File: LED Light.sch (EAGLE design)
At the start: 17 parts, among them J1 AVR_SPI_PRG_6NS, U1 Tiny85-20-SMT

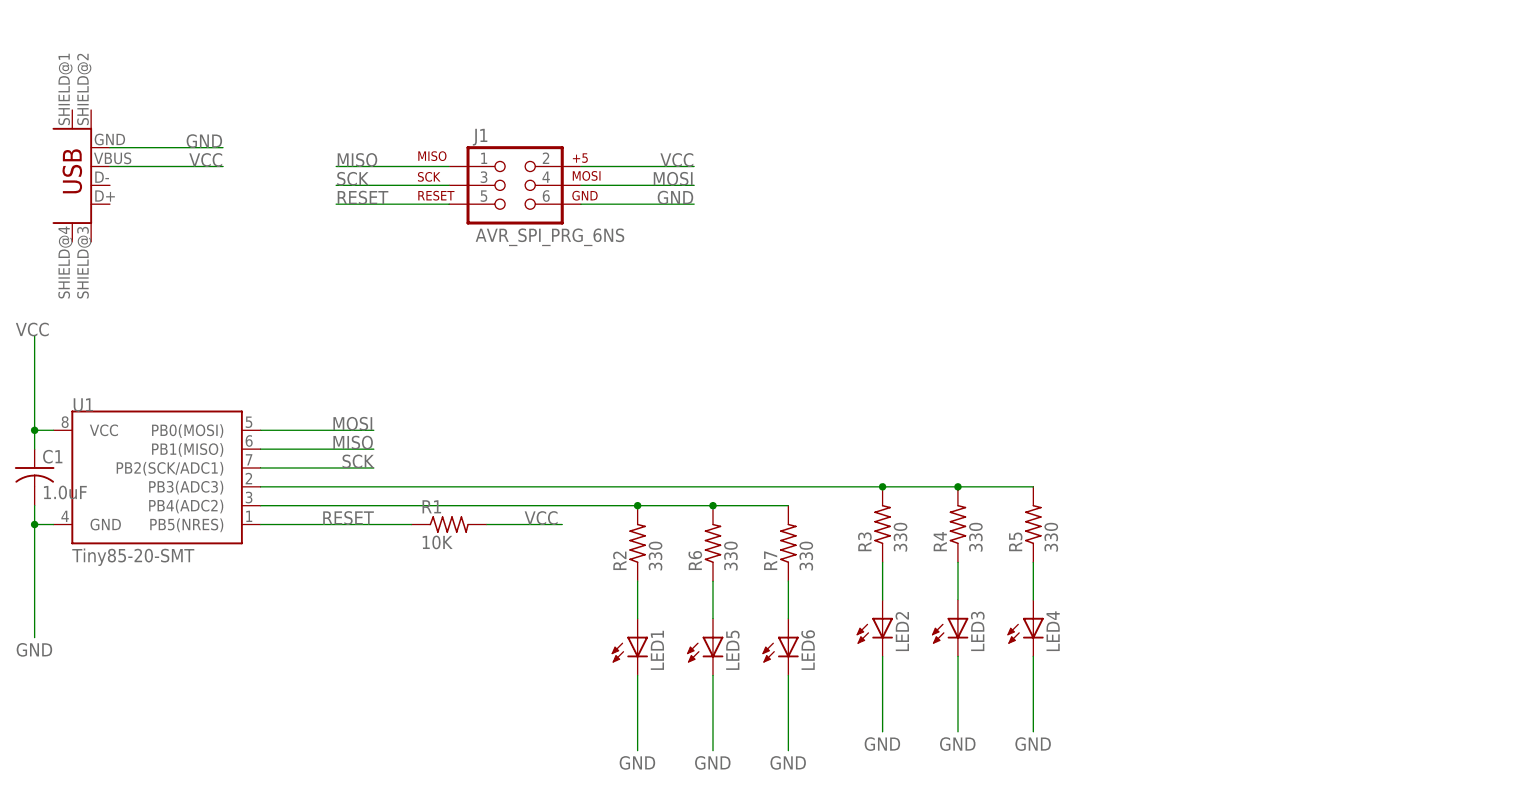
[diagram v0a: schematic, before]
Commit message: Finish initial version of Pac Man board. Generate PNGs for milling.
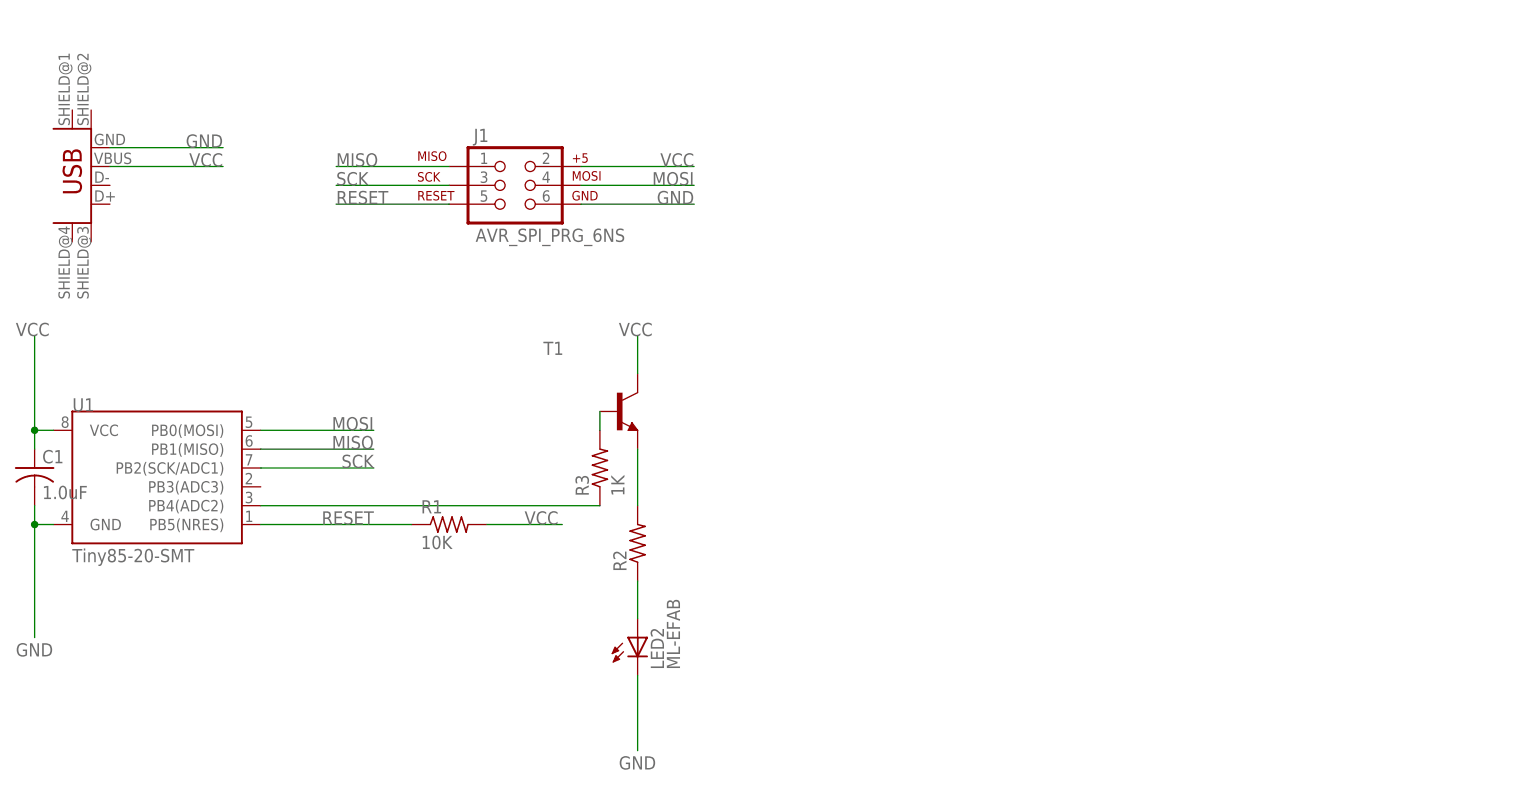
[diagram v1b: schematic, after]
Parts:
- removed LED1, LED3, LED4, LED5, LED6: (no value), led:LEDSMT1206
- removed R4, R5, R6, R7: 330, rcl:R-US_R1206
- added T1: (no value), transistor:MMBT3904LT1-NPN-SOT23-BEC
- JP1: value USB_MINIB -> USB_MINIB-POWER; device fab:USB_MINIB -> LED Light:USB_MINIB-POWER
- LED2: value (none) -> ML-EFAB; device led:LEDSMT1206 -> LED Light:ML-EFAB
- R2: value 330 -> (none)
- R3: value 330 -> 1K
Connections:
- removed net N$5: LED6.A, R7.1
- removed net N$6: LED5.A, R6.1
- removed net N$7: LED3.A, R4.1
- removed net N$8: LED4.A, R5.1
- net GND: now also LED2G$1.C@1; no longer LED1.C, LED2.C, LED3.C, LED4.C, LED5.C, LED6.C
- net N$1: now also T1.E; no longer R6.2, R7.2, U1.PB4(ADC2)
- net N$2: now also T1.B; no longer R4.2, R5.2, U1.PB3(ADC3)
- net N$3: now also LED2G$1.A@1; no longer LED1.A
- net N$4: now also U1.PB4(ADC2); no longer LED2.A
- net VCC: now also T1.C
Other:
- moved on the sheet: R3
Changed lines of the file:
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@@
 <part name="J1" library="SparkFun-Connectors" deviceset="AVR_SPI_PRG_6" device="NS"/>
 <part name="R1" library="rcl" deviceset="R-US_" device="R1206" value="10K"/>
-<part name="R2" library="rcl" deviceset="R-US_" device="R1206" value="330"/>
-<part name="R3" library="rcl" deviceset="R-US_" device="R1206" value="330"/>
-<part name="LED1" library="led" deviceset="LED" device="SMT1206"/>
-<part name="LED2" library="led" deviceset="LED" device="SMT1206"/>
-<part name="JP1" library="fab" deviceset="USB_MINIB" device=""/>
+<part name="R2" library="rcl" deviceset="R-US_" device="R1206"/>
+<part name="JP1" library="LED Light" deviceset="USB_MINIB" device="-POWER"/>
 <part name="C1" library="rcl" deviceset="C-US" device="C1206" value="1.0uF"/>
-<part name="R4" library="rcl" deviceset="R-US_" device="R1206" value="330"/>
-<part name="LED3" library="led" deviceset="LED" device="SMT1206"/>
-<part name="R5" library="rcl" deviceset="R-US_" device="R1206" value="330"/>
-<part name="LED4" library="led" deviceset="LED" device="SMT1206"/>
-<part name="R6" library="rcl" deviceset="R-US_" device="R1206" value="330"/>
-<part name="R7" library="rcl" deviceset="R-US_" device="R1206" value="330"/>
-<part name="LED5" library="led" deviceset="LED" device="SMT1206"/>
-<part name="LED6" library="led" deviceset="LED" device="SMT1206"/>
+<part name="LED2" library="LED Light" deviceset="ML-E" device="FAB"/>
+<part name="T1" library="transistor" deviceset="*-NPN-" device="SOT23-BEC" technology="MMBT3904LT1"/>
+<part name="R3" library="rcl" deviceset="R-US_" device="R1206" value="1K"/>
 </parts>
 <sheets>
@@
 <instance part="R1" gate="G$1" x="66.04" y="33.02"/>
 <instance part="R2" gate="G$1" x="91.44" y="30.48" rot="R90"/>
-<instance part="R3" gate="G$1" x="124.46" y="33.02" rot="R90"/>
-<instance part="LED1" gate="G$1" x="91.44" y="17.78"/>
-<instance part="LED2" gate="G$1" x="124.46" y="20.32"/>
 <instance part="JP1" gate="G$1" x="17.78" y="78.74" rot="R180"/>
 <instance part="C1" gate="G$1" x="10.16" y="40.64"/>
-<instance part="R4" gate="G$1" x="134.62" y="33.02" rot="R90"/>
-<instance part="LED3" gate="G$1" x="134.62" y="20.32"/>
-<instance part="R5" gate="G$1" x="144.78" y="33.02" rot="R90"/>
-<instance part="LED4" gate="G$1" x="144.78" y="20.32"/>
-<instance part="R6" gate="G$1" x="101.6" y="30.48" rot="R90"/>
-<instance part="R7" gate="G$1" x="111.76" y="30.48" rot="R90"/>
-<instance part="LED5" gate="G$1" x="101.6" y="17.78"/>
-<instance part="LED6" gate="G$1" x="111.76" y="17.78"/>
+<instance part="LED2" gate="G$1" x="91.44" y="15.24"/>
+<instance part="T1" gate="G$1" x="88.9" y="48.26"/>
+<instance part="R3" gate="G$1" x="86.36" y="40.64" rot="R90"/>
 </instances>
 <busses>
@@
 <wire x1="20.32" y1="81.28" x2="35.56" y2="81.28" width="0.1524" layer="91"/>
 <label x="35.56" y="81.28" size="1.778" layer="95" rot="MR0"/>
+</segment>
+<segment>
+<pinref part="T1" gate="G$1" pin="C"/>
+<wire x1="91.44" y1="53.34" x2="91.44" y2="58.42" width="0.1524" layer="91"/>
+<label x="88.9" y="58.42" size="1.778" layer="95"/>
 </segment>
 </net>
@@
 </segment>
 <segment>
-<pinref part="LED1" gate="G$1" pin="C"/>
 <wire x1="91.44" y1="12.7" x2="91.44" y2="2.54" width="0.1524" layer="91"/>
 <label x="88.9" y="0" size="1.778" layer="95"/>
-</segment>
-<segment>
-<pinref part="LED2" gate="G$1" pin="C"/>
-<wire x1="124.46" y1="15.24" x2="124.46" y2="5.08" width="0.1524" layer="91"/>
-<label x="121.92" y="2.54" size="1.778" layer="95"/>
-</segment>
-<segment>
-<pinref part="LED3" gate="G$1" pin="C"/>
-<wire x1="134.62" y1="15.24" x2="134.62" y2="5.08" width="0.1524" layer="91"/>
-<label x="132.08" y="2.54" size="1.778" layer="95"/>
-</segment>
-<segment>
-<pinref part="LED4" gate="G$1" pin="C"/>
-<wire x1="144.78" y1="15.24" x2="144.78" y2="5.08" width="0.1524" layer="91"/>
-<label x="142.24" y="2.54" size="1.778" layer="95"/>
-</segment>
-<segment>
-<pinref part="LED5" gate="G$1" pin="C"/>
-<wire x1="101.6" y1="12.7" x2="101.6" y2="2.54" width="0.1524" layer="91"/>
-<label x="99.06" y="0" size="1.778" layer="95"/>
-</segment>
-<segment>
-<pinref part="LED6" gate="G$1" pin="C"/>
-<wire x1="111.76" y1="12.7" x2="111.76" y2="2.54" width="0.1524" layer="91"/>
-<label x="109.22" y="0" size="1.778" layer="95"/>
+<pinref part="LED2" gate="G$1" pin="C@1"/>
 </segment>
 </net>
@@
 </segment>
 </net>
+<net name="N$3" class="0">
+<segment>
+<pinref part="R2" gate="G$1" pin="1"/>
+<wire x1="91.44" y1="20.32" x2="91.44" y2="25.4" width="0.1524" layer="91"/>
+<pinref part="LED2" gate="G$1" pin="A@1"/>
+</segment>
+</net>
 <net name="N$1" class="0">
 <segment>
-<pinref part="U1" gate="G$1" pin="PB4(ADC2)"/>
-<wire x1="40.64" y1="35.56" x2="91.44" y2="35.56" width="0.1524" layer="91"/>
 <pinref part="R2" gate="G$1" pin="2"/>
-<pinref part="R6" gate="G$1" pin="2"/>
-<wire x1="91.44" y1="35.56" x2="101.6" y2="35.56" width="0.1524" layer="91"/>
-<junction x="91.44" y="35.56"/>
-<pinref part="R7" gate="G$1" pin="2"/>
-<wire x1="101.6" y1="35.56" x2="111.76" y2="35.56" width="0.1524" layer="91"/>
-<junction x="101.6" y="35.56"/>
+<pinref part="T1" gate="G$1" pin="E"/>
+<wire x1="91.44" y1="43.18" x2="91.44" y2="35.56" width="0.1524" layer="91"/>
 </segment>
 </net>
 <net name="N$2" class="0">
 <segment>
-<pinref part="U1" gate="G$1" pin="PB3(ADC3)"/>
-<wire x1="40.64" y1="38.1" x2="124.46" y2="38.1" width="0.1524" layer="91"/>
+<pinref part="T1" gate="G$1" pin="B"/>
 <pinref part="R3" gate="G$1" pin="2"/>
-<pinref part="R4" gate="G$1" pin="2"/>
-<wire x1="124.46" y1="38.1" x2="134.62" y2="38.1" width="0.1524" layer="91"/>
-<junction x="124.46" y="38.1"/>
-<pinref part="R5" gate="G$1" pin="2"/>
-<wire x1="134.62" y1="38.1" x2="144.78" y2="38.1" width="0.1524" layer="91"/>
-<junction x="134.62" y="38.1"/>
-</segment>
-</net>
-<net name="N$3" class="0">
-<segment>
-<pinref part="R2" gate="G$1" pin="1"/>
-<pinref part="LED1" gate="G$1" pin="A"/>
-<wire x1="91.44" y1="20.32" x2="91.44" y2="25.4" width="0.1524" layer="91"/>
+<wire x1="86.36" y1="48.26" x2="86.36" y2="45.72" width="0.1524" layer="91"/>
 </segment>
 </net>
 <net name="N$4" class="0">
 <segment>
+<pinref part="U1" gate="G$1" pin="PB4(ADC2)"/>
 <pinref part="R3" gate="G$1" pin="1"/>
-<pinref part="LED2" gate="G$1" pin="A"/>
-<wire x1="124.46" y1="22.86" x2="124.46" y2="27.94" width="0.1524" layer="91"/>
+<wire x1="40.64" y1="35.56" x2="86.36" y2="35.56" width="0.1524" layer="91"/>
 </segment>
 </net>
-<net name="N$7" class="0">
-<segment>
-<pinref part="R4" gate="G$1" pin="1"/>
-<pinref part="LED3" gate="G$1" pin="A"/>
-<wire x1="134.62" y1="27.94" x2="134.62" y2="22.86" width="0.1524" layer="91"/>
-</segment>
-</net>
-<net name="N$8" class="0">
-<segment>
-<pinref part="R5" gate="G$1" pin="1"/>
-<pinref part="LED4" gate="G$1" pin="A"/>
-<wire x1="144.78" y1="27.94" x2="144.78" y2="22.86" width="0.1524" layer="91"/>
-</segment>
-</net>
-<net name="N$5" class="0">
-<segment>
-<pinref part="R7" gate="G$1" pin="1"/>
-<pinref part="LED6" gate="G$1" pin="A"/>
-<wire x1="111.76" y1="25.4" x2="111.76" y2="20.32" width="0.1524" layer="91"/>
-</segment>
-</net>
-<net name="N$6" class="0">
-<segment>
-<pinref part="R6" gate="G$1" pin="1"/>
-<pinref part="LED5" gate="G$1" pin="A"/>
-<wire x1="101.6" y1="25.4" x2="101.6" y2="20.32" width="0.1524" layer="91"/>
-</segment>
-</net>

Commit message: Night-light lamp, including PNGs for milling and PDFs for laser-cutting.
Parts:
- added LED1: ML-EFAB, LED Light:ML-EFAB
- added R4: (no value), rcl:R-US_R1206
- added R6: 49.9K, rcl:R-US_R1206
- added U$1: PHOTOTRANSISTOR-NPN-OP580AD, LED Light:PHOTOTRANSISTOR-NPN-OP580AD
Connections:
- new net N$5: LED1G$1.A@1, R4.1
- new net N$7: R6.1, U$1.C, U1.PB3(ADC3)
- net GND: now also LED1G$1.C@1, U$1.E
- net N$1: now also R4.2
- net VCC: now also R6.2
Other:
- moved on the sheet: J1
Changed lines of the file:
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@@
 <part name="T1" library="transistor" deviceset="*-NPN-" device="SOT23-BEC" technology="MMBT3904LT1"/>
 <part name="R3" library="rcl" deviceset="R-US_" device="R1206" value="1K"/>
+<part name="R4" library="rcl" deviceset="R-US_" device="R1206"/>
+<part name="LED1" library="LED Light" deviceset="ML-E" device="FAB"/>
+<part name="U$1" library="LED Light" deviceset="PHOTOTRANSISTOR-NPN" device="-OP580AD"/>
+<part name="R6" library="rcl" deviceset="R-US_" device="R1206" value="49.9K"/>
 </parts>
 <sheets>
@@
 <instances>
 <instance part="U1" gate="G$1" x="27.94" y="38.1"/>
-<instance part="J1" gate="G$1" x="73.66" y="78.74"/>
+<instance part="J1" gate="G$1" x="88.9" y="88.9"/>
 <instance part="R1" gate="G$1" x="66.04" y="33.02"/>
 <instance part="R2" gate="G$1" x="91.44" y="30.48" rot="R90"/>
@@
 <instance part="T1" gate="G$1" x="88.9" y="48.26"/>
 <instance part="R3" gate="G$1" x="86.36" y="40.64" rot="R90"/>
+<instance part="R4" gate="G$1" x="106.68" y="30.48" rot="R90"/>
+<instance part="LED1" gate="G$1" x="106.68" y="15.24"/>
+<instance part="U$1" gate="G$1" x="76.2" y="50.8"/>
+<instance part="R6" gate="G$1" x="76.2" y="60.96" rot="R90"/>
 </instances>
 <busses>
@@
 <segment>
 <pinref part="J1" gate="G$1" pin="2"/>
-<wire x1="83.82" y1="81.28" x2="99.06" y2="81.28" width="0.1524" layer="91"/>
-<label x="99.06" y="81.28" size="1.778" layer="95" rot="MR0"/>
+<wire x1="99.06" y1="91.44" x2="114.3" y2="91.44" width="0.1524" layer="91"/>
+<label x="114.3" y="91.44" size="1.778" layer="95" rot="MR0"/>
 </segment>
 <segment>
@@
 <label x="88.9" y="58.42" size="1.778" layer="95"/>
 </segment>
+<segment>
+<pinref part="R6" gate="G$1" pin="2"/>
+<wire x1="76.2" y1="66.04" x2="76.2" y2="71.12" width="0.1524" layer="91"/>
+<label x="73.66" y="71.12" size="1.778" layer="95"/>
+</segment>
 </net>
 <net name="MOSI" class="0">
 <segment>
 <pinref part="J1" gate="G$1" pin="4"/>
-<wire x1="83.82" y1="78.74" x2="99.06" y2="78.74" width="0.1524" layer="91"/>
-<label x="99.06" y="78.74" size="1.778" layer="95" rot="MR0"/>
+<wire x1="99.06" y1="88.9" x2="114.3" y2="88.9" width="0.1524" layer="91"/>
+<label x="114.3" y="88.9" size="1.778" layer="95" rot="MR0"/>
 </segment>
 <segment>
@@
 <segment>
 <pinref part="J1" gate="G$1" pin="6"/>
-<wire x1="83.82" y1="76.2" x2="99.06" y2="76.2" width="0.1524" layer="91"/>
-<label x="99.06" y="76.2" size="1.778" layer="95" rot="MR0"/>
+<wire x1="99.06" y1="86.36" x2="114.3" y2="86.36" width="0.1524" layer="91"/>
+<label x="114.3" y="86.36" size="1.778" layer="95" rot="MR0"/>
 </segment>
 <segment>
@@
 <pinref part="LED2" gate="G$1" pin="C@1"/>
 </segment>
+<segment>
+<pinref part="LED1" gate="G$1" pin="C@1"/>
+<wire x1="106.68" y1="12.7" x2="106.68" y2="2.54" width="0.1524" layer="91"/>
+<label x="104.14" y="0" size="1.778" layer="95"/>
+</segment>
+<segment>
+<pinref part="U$1" gate="G$1" pin="E"/>
+<wire x1="76.2" y1="45.72" x2="76.2" y2="40.64" width="0.1524" layer="91"/>
+<label x="73.66" y="38.1" size="1.778" layer="95"/>
+</segment>
 </net>
 <net name="RESET" class="0">
 <segment>
 <pinref part="J1" gate="G$1" pin="5"/>
-<wire x1="66.04" y1="76.2" x2="50.8" y2="76.2" width="0.1524" layer="91"/>
-<label x="50.8" y="76.2" size="1.778" layer="95"/>
+<wire x1="81.28" y1="86.36" x2="66.04" y2="86.36" width="0.1524" layer="91"/>
+<label x="66.04" y="86.36" size="1.778" layer="95"/>
 </segment>
 <segment>
@@
 <segment>
 <pinref part="J1" gate="G$1" pin="3"/>
-<wire x1="66.04" y1="78.74" x2="50.8" y2="78.74" width="0.1524" layer="91"/>
-<label x="50.8" y="78.74" size="1.778" layer="95"/>
+<wire x1="81.28" y1="88.9" x2="66.04" y2="88.9" width="0.1524" layer="91"/>
+<label x="66.04" y="88.9" size="1.778" layer="95"/>
 </segment>
 <segment>
@@
 <segment>
 <pinref part="J1" gate="G$1" pin="1"/>
-<wire x1="66.04" y1="81.28" x2="50.8" y2="81.28" width="0.1524" layer="91"/>
-<label x="50.8" y="81.28" size="1.778" layer="95"/>
+<wire x1="81.28" y1="91.44" x2="66.04" y2="91.44" width="0.1524" layer="91"/>
+<label x="66.04" y="91.44" size="1.778" layer="95"/>
 </segment>
 <segment>
@@
 <pinref part="T1" gate="G$1" pin="E"/>
 <wire x1="91.44" y1="43.18" x2="91.44" y2="35.56" width="0.1524" layer="91"/>
+<pinref part="R4" gate="G$1" pin="2"/>
+<wire x1="91.44" y1="35.56" x2="106.68" y2="35.56" width="0.1524" layer="91"/>
+<junction x="91.44" y="35.56"/>
 </segment>
 </net>
@@
 </segment>
 </net>
+<net name="N$5" class="0">
+<segment>
+<pinref part="R4" gate="G$1" pin="1"/>
+<pinref part="LED1" gate="G$1" pin="A@1"/>
+<wire x1="106.68" y1="25.4" x2="106.68" y2="20.32" width="0.1524" layer="91"/>
+</segment>
+</net>
+<net name="N$7" class="0">
+<segment>
+<pinref part="U$1" gate="G$1" pin="C"/>
+<pinref part="R6" gate="G$1" pin="1"/>
+<wire x1="76.2" y1="55.88" x2="66.04" y2="55.88" width="0.1524" layer="91"/>
+<wire x1="66.04" y1="55.88" x2="66.04" y2="38.1" width="0.1524" layer="91"/>
+<junction x="76.2" y="55.88"/>
+<pinref part="U1" gate="G$1" pin="PB3(ADC3)"/>
+<wire x1="66.04" y1="38.1" x2="40.64" y2="38.1" width="0.1524" layer="91"/>
+</segment>
+</net>

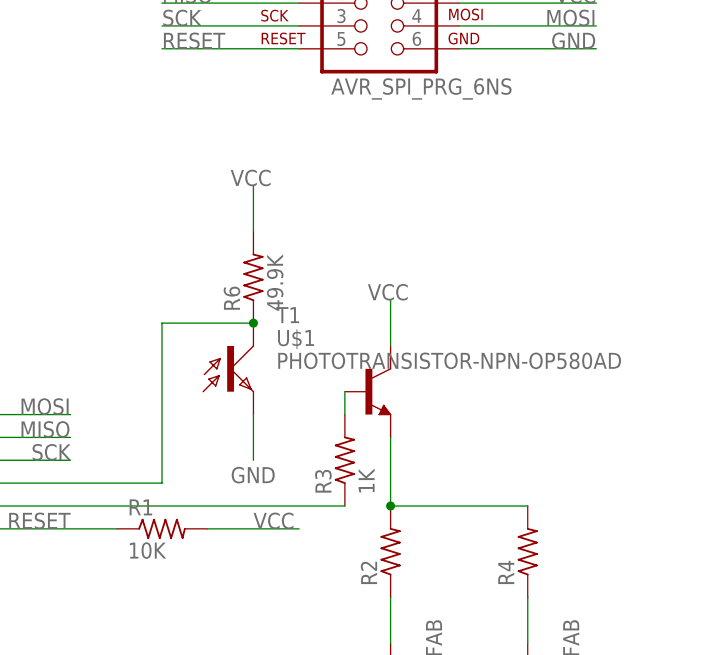
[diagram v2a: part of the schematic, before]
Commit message: Initial work on board layout. Still missing mic circuit.
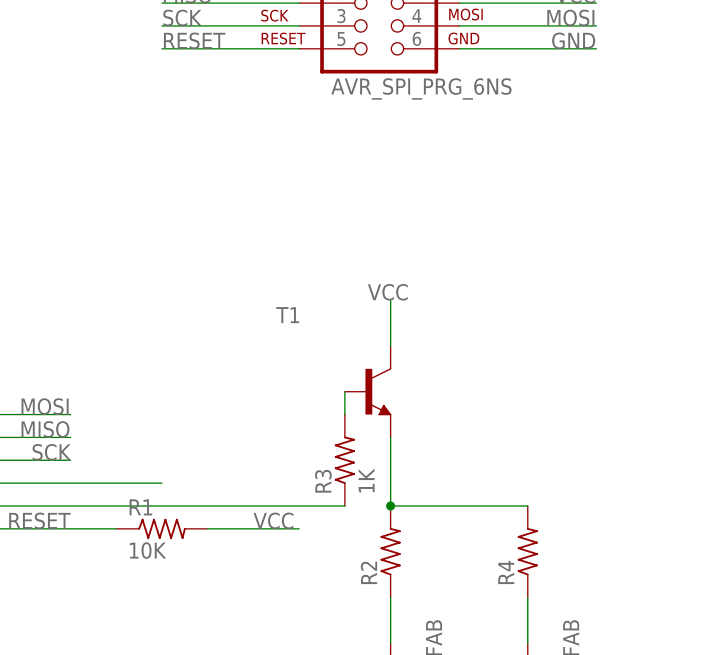
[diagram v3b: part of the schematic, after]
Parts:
- removed R6: 49.9K, rcl:R-US_R1206
- removed U$1: PHOTOTRANSISTOR-NPN-OP580AD, LED Light:PHOTOTRANSISTOR-NPN-OP580AD
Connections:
- net GND: no longer U$1.E
- net N$7: no longer R6.1, U$1.C
- net VCC: no longer R6.2
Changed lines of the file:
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@@
 <part name="R4" library="rcl" deviceset="R-US_" device="R1206"/>
 <part name="LED1" library="LED Light" deviceset="ML-E" device="FAB"/>
-<part name="U$1" library="LED Light" deviceset="PHOTOTRANSISTOR-NPN" device="-OP580AD"/>
-<part name="R6" library="rcl" deviceset="R-US_" device="R1206" value="49.9K"/>
 </parts>
 <sheets>
@@
 <instance part="R4" gate="G$1" x="106.68" y="30.48" rot="R90"/>
 <instance part="LED1" gate="G$1" x="106.68" y="15.24"/>
-<instance part="U$1" gate="G$1" x="76.2" y="50.8"/>
-<instance part="R6" gate="G$1" x="76.2" y="60.96" rot="R90"/>
 </instances>
 <busses>
@@
 <wire x1="91.44" y1="53.34" x2="91.44" y2="58.42" width="0.1524" layer="91"/>
 <label x="88.9" y="58.42" size="1.778" layer="95"/>
-</segment>
-<segment>
-<pinref part="R6" gate="G$1" pin="2"/>
-<wire x1="76.2" y1="66.04" x2="76.2" y2="71.12" width="0.1524" layer="91"/>
-<label x="73.66" y="71.12" size="1.778" layer="95"/>
 </segment>
 </net>
@@
 <wire x1="106.68" y1="12.7" x2="106.68" y2="2.54" width="0.1524" layer="91"/>
 <label x="104.14" y="0" size="1.778" layer="95"/>
-</segment>
-<segment>
-<pinref part="U$1" gate="G$1" pin="E"/>
-<wire x1="76.2" y1="45.72" x2="76.2" y2="40.64" width="0.1524" layer="91"/>
-<label x="73.66" y="38.1" size="1.778" layer="95"/>
 </segment>
 </net>
@@
 <net name="N$7" class="0">
 <segment>
-<pinref part="U$1" gate="G$1" pin="C"/>
-<pinref part="R6" gate="G$1" pin="1"/>
-<wire x1="76.2" y1="55.88" x2="66.04" y2="55.88" width="0.1524" layer="91"/>
-<wire x1="66.04" y1="55.88" x2="66.04" y2="38.1" width="0.1524" layer="91"/>
-<junction x="76.2" y="55.88"/>
 <pinref part="U1" gate="G$1" pin="PB3(ADC3)"/>
 <wire x1="66.04" y1="38.1" x2="40.64" y2="38.1" width="0.1524" layer="91"/>
